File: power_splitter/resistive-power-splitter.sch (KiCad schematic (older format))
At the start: 36 parts, among them J1 Conn_01x02, J10 Conn_01x02, J11 Conn_01x02, J12 Conn_01x02, J2 Conn_01x02, J3 Conn_01x02, J4 Conn_01x02, J5 Conn_01x02, J6 Conn_01x02, J7 Conn_01x02, J8 Conn_01x02, J9 Conn_01x02

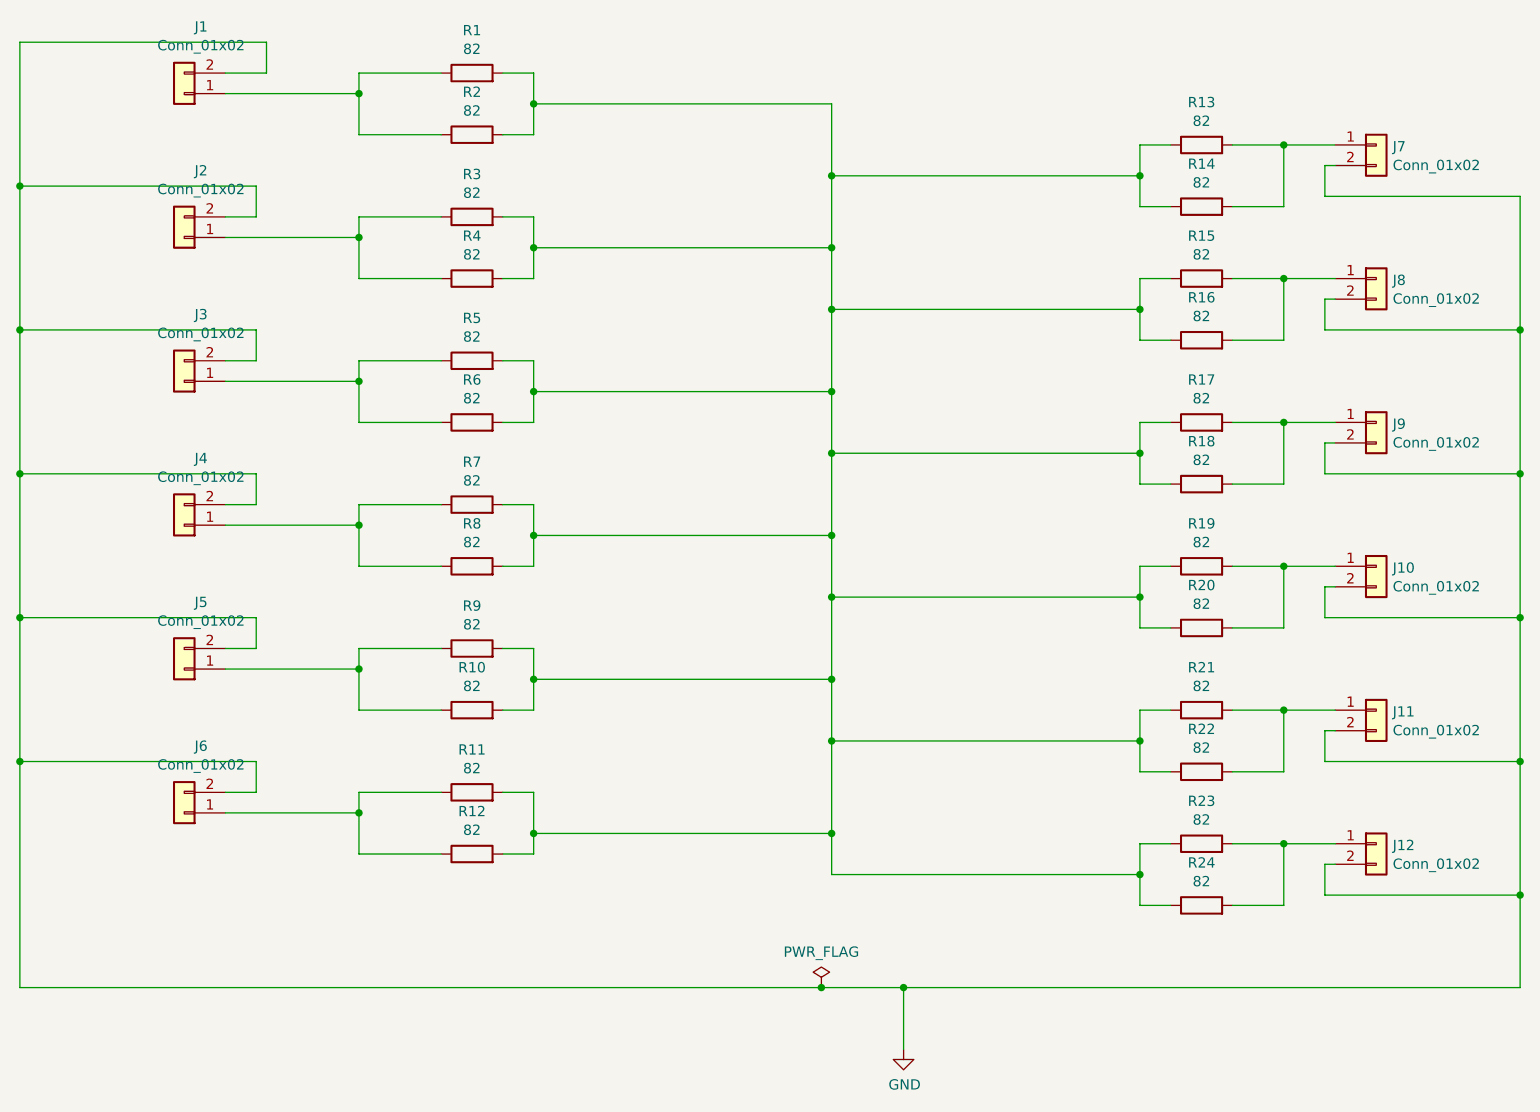
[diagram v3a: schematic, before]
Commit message: power splitter: update schematic for v0.2
Switch to using only one resistor per output.

Ideal resistor value: 41.67 Ω
Available resistor vaulue: 41.2 Ω
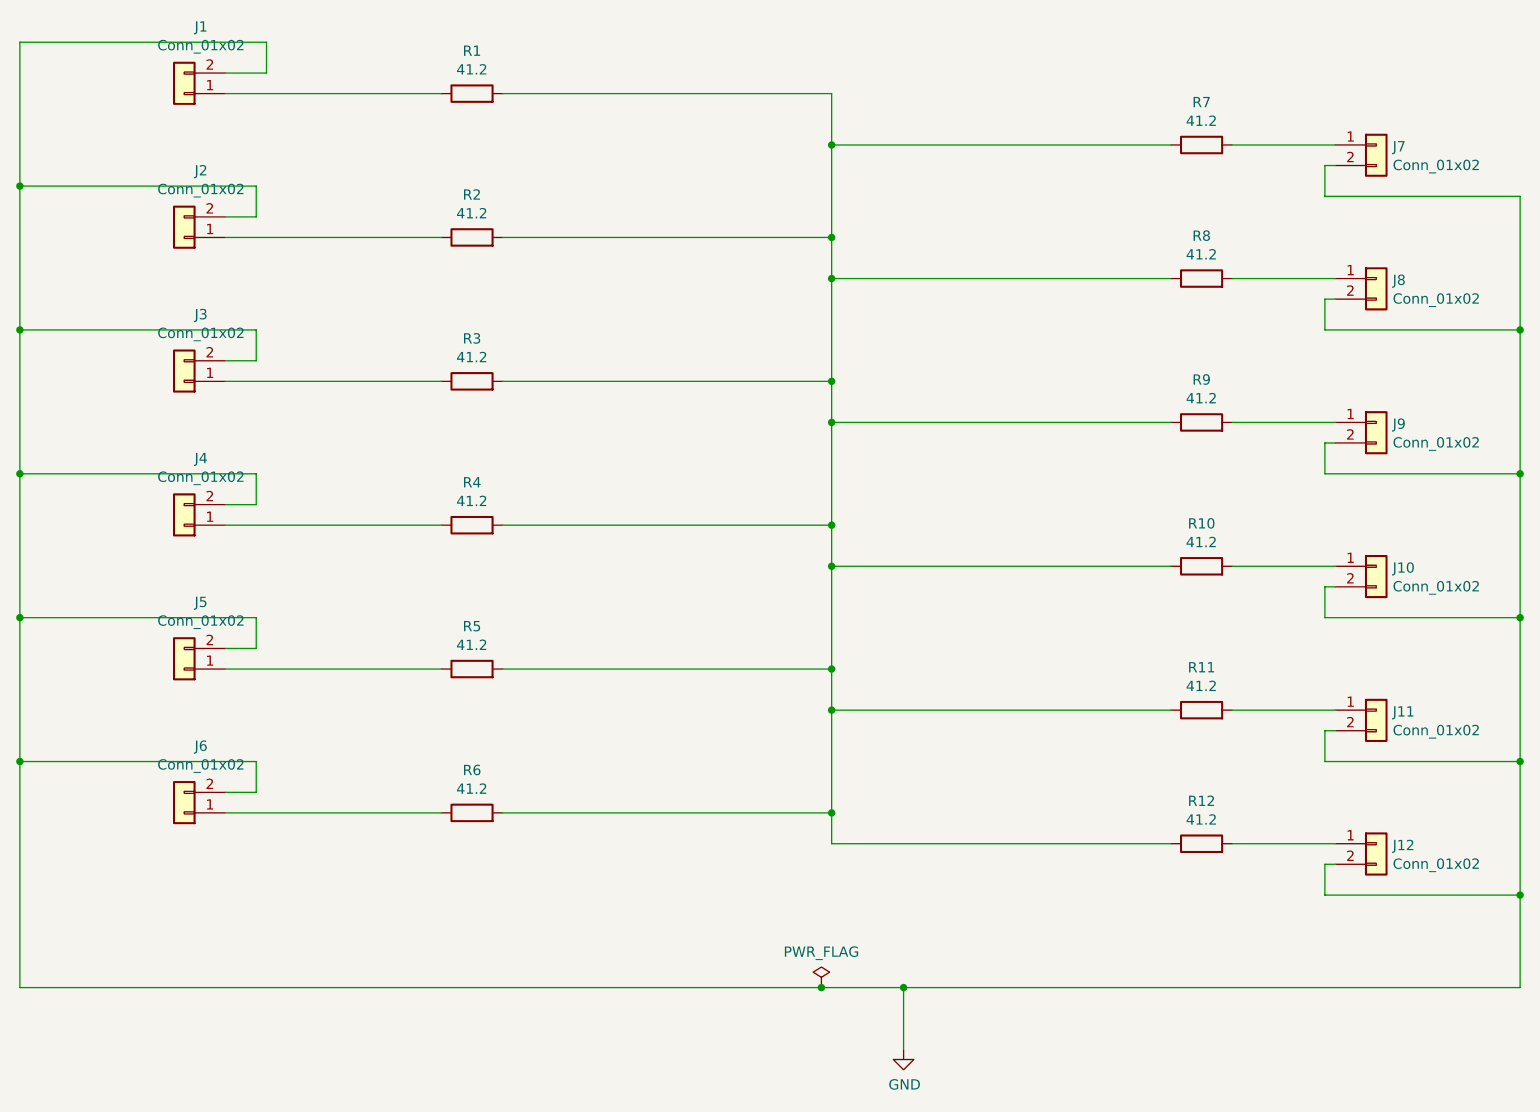
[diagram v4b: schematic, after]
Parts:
- removed R10, R12, R14, R16, R18, R2, R20, R22, R24, R4, R6, R8: 82, Resistor_SMD:R_0402_1005Metric, symbol Device:R
- J1, J10, J11, J12, J2, J3, J4, J5, J6, J7, J8, J9: LCSC C411575 -> (none)
- R1: value 82 -> 41.2; LCSC C25136 -> C270602
- R10: renamed from R19; value 82 -> 41.2; LCSC C25136 -> C270602
- R11: renamed from R21; value 82 -> 41.2; LCSC C25136 -> C270602
- R12: renamed from R23; value 82 -> 41.2; LCSC C25136 -> C270602
- R2: renamed from R3; value 82 -> 41.2; LCSC C25136 -> C270602
- R3: renamed from R5; value 82 -> 41.2; LCSC C25136 -> C270602
- R4: renamed from R7; value 82 -> 41.2; LCSC C25136 -> C270602
- R5: renamed from R9; value 82 -> 41.2; LCSC C25136 -> C270602
- R6: renamed from R11; value 82 -> 41.2; LCSC C25136 -> C270602
- R7: renamed from R13; value 82 -> 41.2; LCSC C25136 -> C270602
- R8: renamed from R15; value 82 -> 41.2; LCSC C25136 -> C270602
- R9: renamed from R17; value 82 -> 41.2; LCSC C25136 -> C270602
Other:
- moved on the sheet: R1, R2, R3, R4, R5, R6

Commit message: power splitter: add part number for new SMA connector & datasheets
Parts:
- J1, J10, J11, J12, J2, J3, J4, J5, J6, J7, J8, J9: LCSC (none) -> C1509227
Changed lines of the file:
@@
 F 2 "Connector_Coaxial:SMA_Amphenol_132203-12_Horizontal" H 1650 1450 50  0001 C CNN
 F 3 "~" H 1650 1450 50  0001 C CNN
-F 4 "" H 1650 1450 50  0001 C CNN "LCSC"
+F 4 "C1509227" H 1650 1450 50  0001 C CNN "LCSC"
 	1    1650 1450
 	-1   0    0    1
@@
 F 2 "Connector_Coaxial:SMA_Amphenol_132203-12_Horizontal" H 1650 2150 50  0001 C CNN
 F 3 "~" H 1650 2150 50  0001 C CNN
-F 4 "" H 1650 2150 50  0001 C CNN "LCSC"
+F 4 "C1509227" H 1650 2150 50  0001 C CNN "LCSC"
 	1    1650 2150
 	-1   0    0    1
@@
 F 2 "Connector_Coaxial:SMA_Amphenol_132203-12_Horizontal" H 1650 2850 50  0001 C CNN
 F 3 "~" H 1650 2850 50  0001 C CNN
-F 4 "" H 1650 2850 50  0001 C CNN "LCSC"
+F 4 "C1509227" H 1650 2850 50  0001 C CNN "LCSC"
 	1    1650 2850
 	-1   0    0    1
@@
 F 2 "Connector_Coaxial:SMA_Amphenol_132203-12_Horizontal" H 1650 3550 50  0001 C CNN
 F 3 "~" H 1650 3550 50  0001 C CNN
-F 4 "" H 1650 3550 50  0001 C CNN "LCSC"
+F 4 "C1509227" H 1650 3550 50  0001 C CNN "LCSC"
 	1    1650 3550
 	-1   0    0    1
@@
 F 2 "Connector_Coaxial:SMA_Amphenol_132203-12_Horizontal" H 1650 4250 50  0001 C CNN
 F 3 "~" H 1650 4250 50  0001 C CNN
-F 4 "" H 1650 4250 50  0001 C CNN "LCSC"
+F 4 "C1509227" H 1650 4250 50  0001 C CNN "LCSC"
 	1    1650 4250
 	-1   0    0    1
@@
 F 2 "Connector_Coaxial:SMA_Amphenol_132203-12_Horizontal" H 1650 4950 50  0001 C CNN
 F 3 "~" H 1650 4950 50  0001 C CNN
-F 4 "" H 1650 4950 50  0001 C CNN "LCSC"
+F 4 "C1509227" H 1650 4950 50  0001 C CNN "LCSC"
 	1    1650 4950
 	-1   0    0    1
@@
 F 2 "Connector_Coaxial:SMA_Amphenol_132203-12_Horizontal" H 7450 2350 50  0001 C CNN
 F 3 "~" H 7450 2350 50  0001 C CNN
-F 4 "" H 7450 2350 50  0001 C CNN "LCSC"
+F 4 "C1509227" H 7450 2350 50  0001 C CNN "LCSC"
 	1    7450 2350
 	1    0    0    -1
@@
 F 2 "Connector_Coaxial:SMA_Amphenol_132203-12_Horizontal" H 7450 3050 50  0001 C CNN
 F 3 "~" H 7450 3050 50  0001 C CNN
-F 4 "" H 7450 3050 50  0001 C CNN "LCSC"
+F 4 "C1509227" H 7450 3050 50  0001 C CNN "LCSC"
 	1    7450 3050
 	1    0    0    -1
@@
 F 2 "Connector_Coaxial:SMA_Amphenol_132203-12_Horizontal" H 7450 3750 50  0001 C CNN
 F 3 "~" H 7450 3750 50  0001 C CNN
-F 4 "" H 7450 3750 50  0001 C CNN "LCSC"
+F 4 "C1509227" H 7450 3750 50  0001 C CNN "LCSC"
 	1    7450 3750
 	1    0    0    -1
@@
 F 2 "Connector_Coaxial:SMA_Amphenol_132203-12_Horizontal" H 7450 4450 50  0001 C CNN
 F 3 "~" H 7450 4450 50  0001 C CNN
-F 4 "" H 7450 4450 50  0001 C CNN "LCSC"
+F 4 "C1509227" H 7450 4450 50  0001 C CNN "LCSC"
 	1    7450 4450
 	1    0    0    -1
@@
 F 2 "Connector_Coaxial:SMA_Amphenol_132203-12_Horizontal" H 7450 1700 50  0001 C CNN
 F 3 "~" H 7450 1700 50  0001 C CNN
-F 4 "" H 7450 1700 50  0001 C CNN "LCSC"
+F 4 "C1509227" H 7450 1700 50  0001 C CNN "LCSC"
 	1    7450 1700
 	1    0    0    -1
@@
 F 2 "Connector_Coaxial:SMA_Amphenol_132203-12_Horizontal" H 7450 5100 50  0001 C CNN
 F 3 "~" H 7450 5100 50  0001 C CNN
-F 4 "" H 7450 5100 50  0001 C CNN "LCSC"
+F 4 "C1509227" H 7450 5100 50  0001 C CNN "LCSC"
 	1    7450 5100
 	1    0    0    -1

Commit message: power splitter: use custom footprint with associated 3d model for SMA connectors
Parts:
- J1, J10, J11, J12, J2, J3, J4, J5, J6, J7, J8, J9: footprint Connector_Coaxial:SMA_Amphenol_132203-12_Horizontal -> custom_library:SMA_HJ-SMA003
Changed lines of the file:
@@
 F 0 "J1" H 1568 1125 50  0000 C CNN
 F 1 "Conn_01x02" H 1568 1216 50  0000 C CNN
-F 2 "Connector_Coaxial:SMA_Amphenol_132203-12_Horizontal" H 1650 1450 50  0001 C CNN
+F 2 "custom_library:SMA_HJ-SMA003" H 1650 1450 50  0001 C CNN
 F 3 "~" H 1650 1450 50  0001 C CNN
 F 4 "C1509227" H 1650 1450 50  0001 C CNN "LCSC"
@@
 F 0 "J2" H 1568 1825 50  0000 C CNN
 F 1 "Conn_01x02" H 1568 1916 50  0000 C CNN
-F 2 "Connector_Coaxial:SMA_Amphenol_132203-12_Horizontal" H 1650 2150 50  0001 C CNN
+F 2 "custom_library:SMA_HJ-SMA003" H 1650 2150 50  0001 C CNN
 F 3 "~" H 1650 2150 50  0001 C CNN
 F 4 "C1509227" H 1650 2150 50  0001 C CNN "LCSC"
@@
 F 0 "J3" H 1568 2525 50  0000 C CNN
 F 1 "Conn_01x02" H 1568 2616 50  0000 C CNN
-F 2 "Connector_Coaxial:SMA_Amphenol_132203-12_Horizontal" H 1650 2850 50  0001 C CNN
+F 2 "custom_library:SMA_HJ-SMA003" H 1650 2850 50  0001 C CNN
 F 3 "~" H 1650 2850 50  0001 C CNN
 F 4 "C1509227" H 1650 2850 50  0001 C CNN "LCSC"
@@
 F 0 "J4" H 1568 3225 50  0000 C CNN
 F 1 "Conn_01x02" H 1568 3316 50  0000 C CNN
-F 2 "Connector_Coaxial:SMA_Amphenol_132203-12_Horizontal" H 1650 3550 50  0001 C CNN
+F 2 "custom_library:SMA_HJ-SMA003" H 1650 3550 50  0001 C CNN
 F 3 "~" H 1650 3550 50  0001 C CNN
 F 4 "C1509227" H 1650 3550 50  0001 C CNN "LCSC"
@@
 F 0 "J5" H 1568 3925 50  0000 C CNN
 F 1 "Conn_01x02" H 1568 4016 50  0000 C CNN
-F 2 "Connector_Coaxial:SMA_Amphenol_132203-12_Horizontal" H 1650 4250 50  0001 C CNN
+F 2 "custom_library:SMA_HJ-SMA003" H 1650 4250 50  0001 C CNN
 F 3 "~" H 1650 4250 50  0001 C CNN
 F 4 "C1509227" H 1650 4250 50  0001 C CNN "LCSC"
@@
 F 0 "J6" H 1568 4625 50  0000 C CNN
 F 1 "Conn_01x02" H 1568 4716 50  0000 C CNN
-F 2 "Connector_Coaxial:SMA_Amphenol_132203-12_Horizontal" H 1650 4950 50  0001 C CNN
+F 2 "custom_library:SMA_HJ-SMA003" H 1650 4950 50  0001 C CNN
 F 3 "~" H 1650 4950 50  0001 C CNN
 F 4 "C1509227" H 1650 4950 50  0001 C CNN "LCSC"
@@
 F 0 "J8" H 7530 2342 50  0000 L CNN
 F 1 "Conn_01x02" H 7530 2251 50  0000 L CNN
-F 2 "Connector_Coaxial:SMA_Amphenol_132203-12_Horizontal" H 7450 2350 50  0001 C CNN
+F 2 "custom_library:SMA_HJ-SMA003" H 7450 2350 50  0001 C CNN
 F 3 "~" H 7450 2350 50  0001 C CNN
 F 4 "C1509227" H 7450 2350 50  0001 C CNN "LCSC"
@@
 F 0 "J9" H 7530 3042 50  0000 L CNN
 F 1 "Conn_01x02" H 7530 2951 50  0000 L CNN
-F 2 "Connector_Coaxial:SMA_Amphenol_132203-12_Horizontal" H 7450 3050 50  0001 C CNN
+F 2 "custom_library:SMA_HJ-SMA003" H 7450 3050 50  0001 C CNN
 F 3 "~" H 7450 3050 50  0001 C CNN
 F 4 "C1509227" H 7450 3050 50  0001 C CNN "LCSC"
@@
 F 0 "J10" H 7530 3742 50  0000 L CNN
 F 1 "Conn_01x02" H 7530 3651 50  0000 L CNN
-F 2 "Connector_Coaxial:SMA_Amphenol_132203-12_Horizontal" H 7450 3750 50  0001 C CNN
+F 2 "custom_library:SMA_HJ-SMA003" H 7450 3750 50  0001 C CNN
 F 3 "~" H 7450 3750 50  0001 C CNN
 F 4 "C1509227" H 7450 3750 50  0001 C CNN "LCSC"
@@
 F 0 "J11" H 7530 4442 50  0000 L CNN
 F 1 "Conn_01x02" H 7530 4351 50  0000 L CNN
-F 2 "Connector_Coaxial:SMA_Amphenol_132203-12_Horizontal" H 7450 4450 50  0001 C CNN
+F 2 "custom_library:SMA_HJ-SMA003" H 7450 4450 50  0001 C CNN
 F 3 "~" H 7450 4450 50  0001 C CNN
 F 4 "C1509227" H 7450 4450 50  0001 C CNN "LCSC"
@@
 F 0 "J7" H 7530 1692 50  0000 L CNN
 F 1 "Conn_01x02" H 7530 1601 50  0000 L CNN
-F 2 "Connector_Coaxial:SMA_Amphenol_132203-12_Horizontal" H 7450 1700 50  0001 C CNN
+F 2 "custom_library:SMA_HJ-SMA003" H 7450 1700 50  0001 C CNN
 F 3 "~" H 7450 1700 50  0001 C CNN
 F 4 "C1509227" H 7450 1700 50  0001 C CNN "LCSC"
@@
 F 0 "J12" H 7530 5092 50  0000 L CNN
 F 1 "Conn_01x02" H 7530 5001 50  0000 L CNN
-F 2 "Connector_Coaxial:SMA_Amphenol_132203-12_Horizontal" H 7450 5100 50  0001 C CNN
+F 2 "custom_library:SMA_HJ-SMA003" H 7450 5100 50  0001 C CNN
 F 3 "~" H 7450 5100 50  0001 C CNN
 F 4 "C1509227" H 7450 5100 50  0001 C CNN "LCSC"
